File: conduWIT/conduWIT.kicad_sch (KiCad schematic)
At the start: 26 parts, among them J1 Conn_01x10, J10 SJ1-2503A, J2 Conn_01x08, J3 Conn_01x08, J4 Conn_01x06, J5 SJ1-2503A, J6 SJ1-2503A, J7 SJ1-2503A, J8 SJ1-2503A, J9 SJ1-2503A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

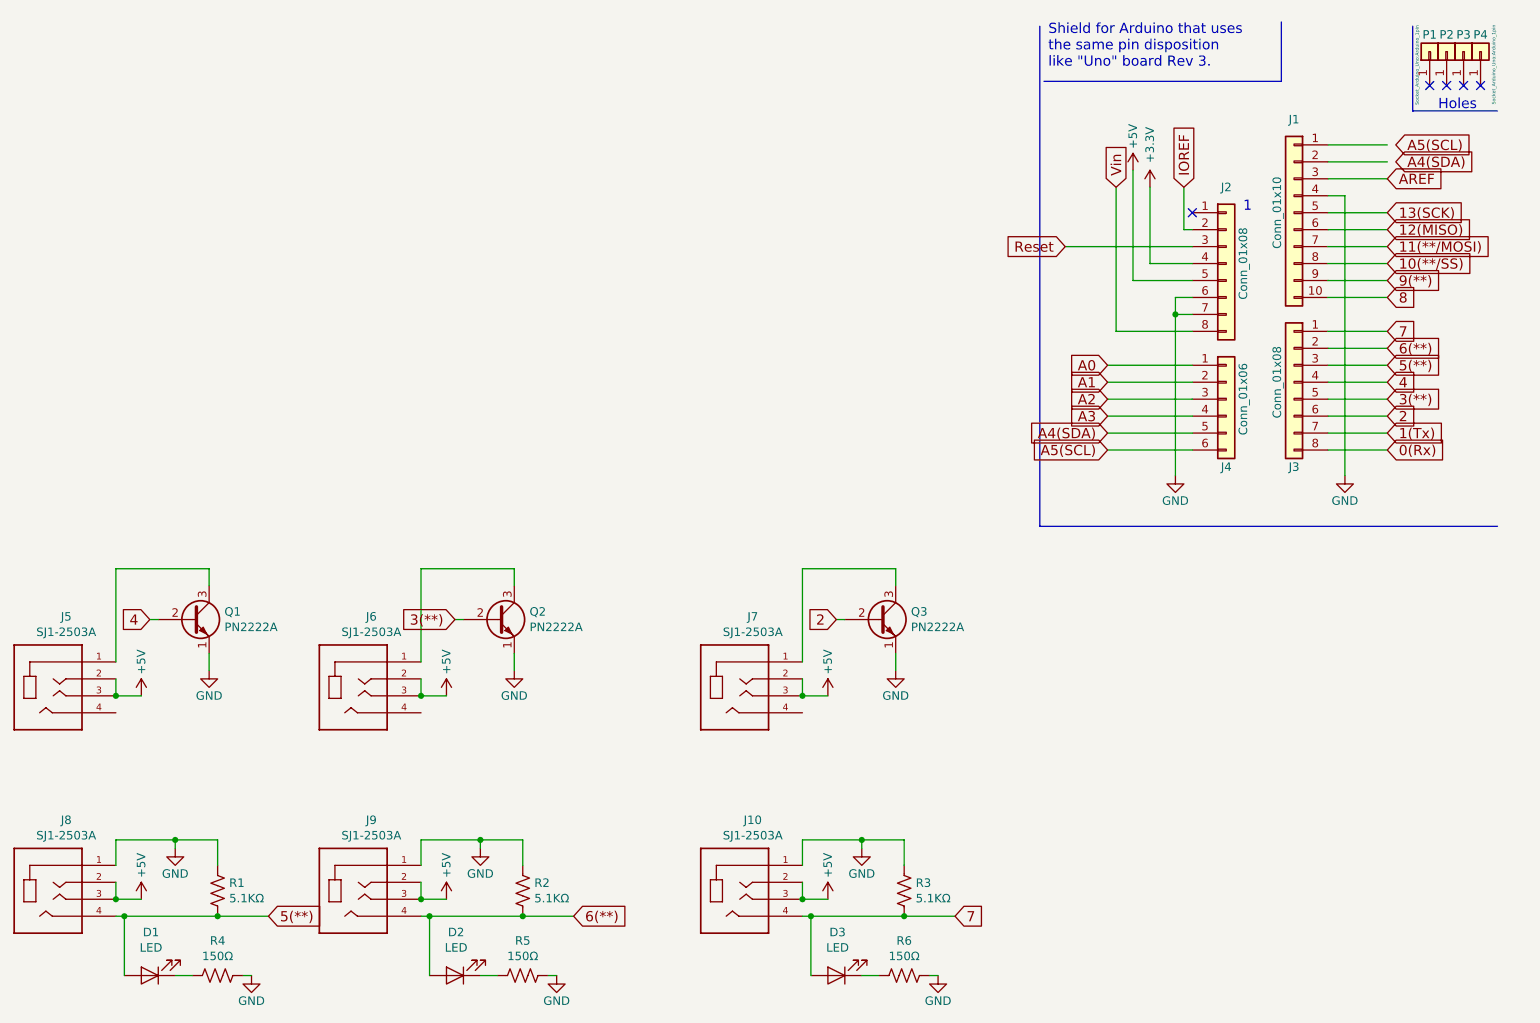
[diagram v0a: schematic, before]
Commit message: Clean up schematic
Fix islands on bottom of PCB
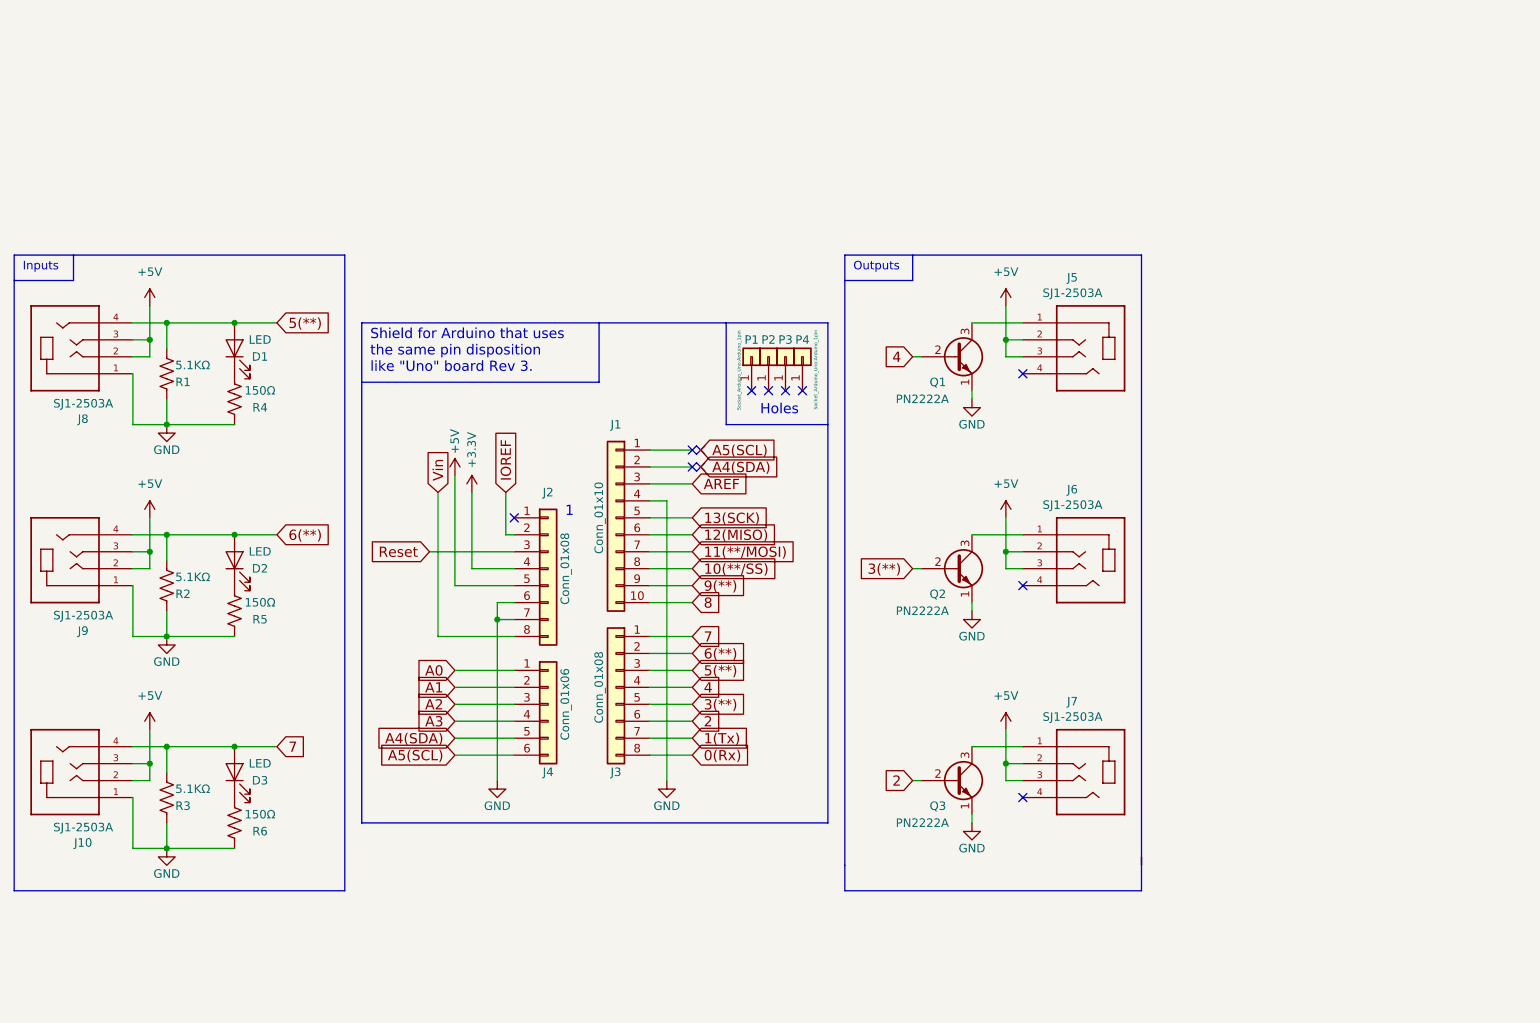
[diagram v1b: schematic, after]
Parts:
- removed D1: LED, conduWIT_parts:LED_D5.0mm, symbol conduWIT_parts:LED
- removed J5, J8: SJ1-2503A, conduWIT_parts:CUI_SJ1-2503A, symbol conduWIT_parts:SJ1-2503A
- removed Q1: PN2222A, conduWIT_parts:TO-92_Inline, symbol conduWIT_parts:PN2222A
- removed R1: 5.1KΩ, conduWIT_parts:R_Axial_DIN0207_L6.3mm_D2.5mm_P7.62mm_Horizontal, symbol conduWIT_parts:10KΩ
- removed R4: 150Ω, conduWIT_parts:R_Axial_DIN0207_L6.3mm_D2.5mm_P7.62mm_Horizontal, symbol conduWIT_parts:30Ω
- added D3: LED, conduWIT_parts:LED_D5.0mm, symbol conduWIT_parts:LED
- added J10, J7: SJ1-2503A, conduWIT_parts:CUI_SJ1-2503A, symbol conduWIT_parts:SJ1-2503A
- added Q3: PN2222A, conduWIT_parts:TO-92_Inline, symbol conduWIT_parts:PN2222A
- added R3: 5.1KΩ, conduWIT_parts:R_Axial_DIN0207_L6.3mm_D2.5mm_P7.62mm_Horizontal, symbol conduWIT_parts:10KΩ
- added R6: 150Ω, conduWIT_parts:R_Axial_DIN0207_L6.3mm_D2.5mm_P7.62mm_Horizontal, symbol conduWIT_parts:30Ω
- renumbered D3 to D1, J7 to J5, J10 to J8, Q3 to Q1, R3 to R1, R6 to R4
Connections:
- net +5V: now also J10.2, J10.3, J7.2, J7.3
- net 2: now also Q3.2 (B); no longer Q1.2 (B)
- net 4: now also Q1.2 (B)
- net 5(**): now also D1.2 (A), J8.4, R1.2
- net 7: now also D3.2 (A), J10.4, R3.2; no longer D1.2 (A), J8.4, R1.2
- net GND: now also J10.1, Q3.1 (E), R3.1, R6.1
- new net: J7.1, Q3.3 (C)
- new net: D3.1 (K), R6.2
- no-connect marks 5 -> 12
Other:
- note added: "Inputs"
- note added: "Outputs"
- moved on the sheet: D1, J1, J2, J3, J4, J5, J8, P1, P2, P3, P4, Q1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
